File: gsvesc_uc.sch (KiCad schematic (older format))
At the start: 13 parts, among them U1 STM32F405RGTx, Y1 X50328MSB2GI

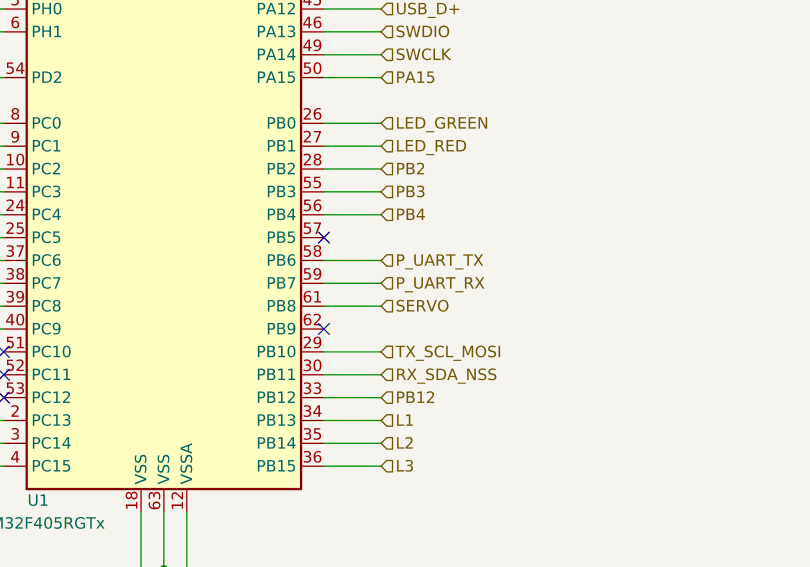
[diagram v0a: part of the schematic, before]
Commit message: Planes und Vias
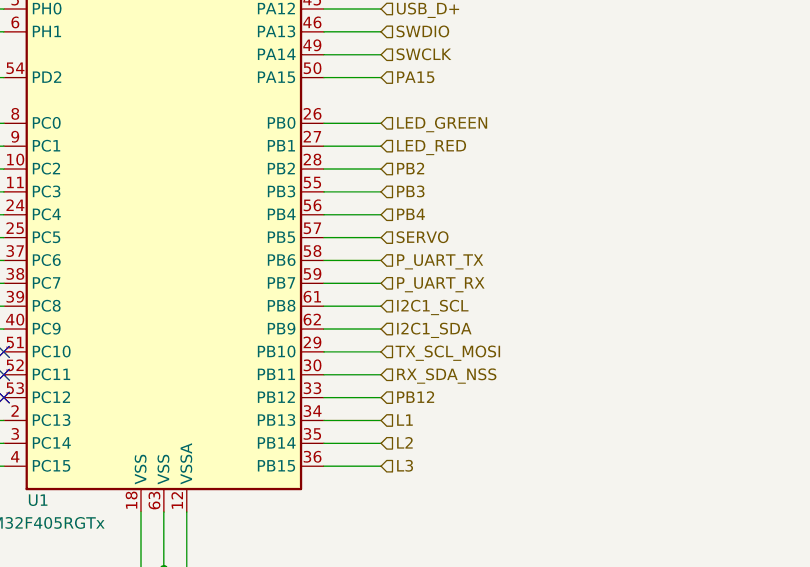
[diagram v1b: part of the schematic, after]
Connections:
- net SERVO: now also U1.57 (PB5); no longer U1.61 (PB8)
- net I2C1_SDA: now reaches U1.62 (PB9)
- new net I2C1_SCL: U1.61 (PB8)
- no-connect marks 5 -> 3
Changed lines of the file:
@@
 Comment4 ""
 $EndDescr
-$Comp
-L MCU_ST_STM32F4:STM32F405RGTx U1
-U 1 1 5BFF9EEA
-P 4150 4200
-F 0 "U1" H 3600 2450 50  0000 C CNN
-F 1 "STM32F405RGTx" H 3600 2350 50  0000 C CNN
-F 2 "Package_QFP:LQFP-64_10x10mm_P0.5mm" H 3550 2500 50  0001 R CNN
-F 3 "http://www.st.com/st-web-ui/static/active/en/resource/technical/document/datasheet/DM00037051.pdf" H 4150 4200 50  0001 C CNN
-	1    4150 4200
-	1    0    0    -1
-$EndComp
 Text HLabel 5100 2600 2    50   Input ~ 0
 VOLTAGE_1
@@
 Text HLabel 5100 4400 2    50   Input ~ 0
 LED_RED
-Text HLabel 5100 5100 2    50   Input ~ 0
+Text HLabel 5100 4800 2    50   Input ~ 0
 SERVO
 Text HLabel 5100 5300 2    50   Input ~ 0
@@
 	4850 5000 5100 5000
 Wire Wire Line
-	5100 5100 4850 5100
+	5100 4800 4850 4800
 Wire Wire Line
 	5100 5300 4850 5300
@@
 Text HLabel 3150 5200 0    50   Input ~ 0
 SENS_FILTER_ON
-NoConn ~ 4850 4800
-NoConn ~ 4850 5200
 NoConn ~ 3450 5300
 NoConn ~ 3450 5400
@@
 	1700 3700 1900 3700
 Connection ~ 1900 3700
+$Comp
+L MCU_ST_STM32F4:STM32F405RGTx U1
+U 1 1 5BFF9EEA
+P 4150 4200
+F 0 "U1" H 3600 2450 50  0000 C CNN
+F 1 "STM32F405RGTx" H 3600 2350 50  0000 C CNN
+F 2 "Package_QFP:LQFP-64_10x10mm_P0.5mm" H 3550 2500 50  0001 R CNN
+F 3 "http://www.st.com/st-web-ui/static/active/en/resource/technical/document/datasheet/DM00037051.pdf" H 4150 4200 50  0001 C CNN
+	1    4150 4200
+	1    0    0    -1
+$EndComp
+Wire Wire Line
+	4850 5100 5100 5100
+Wire Wire Line
+	4850 5200 5100 5200
+Text HLabel 5100 5100 2    50   Input ~ 0
+I2C1_SCL
+Text HLabel 5100 5200 2    50   Input ~ 0
+I2C1_SDA
 $EndSCHEMATC

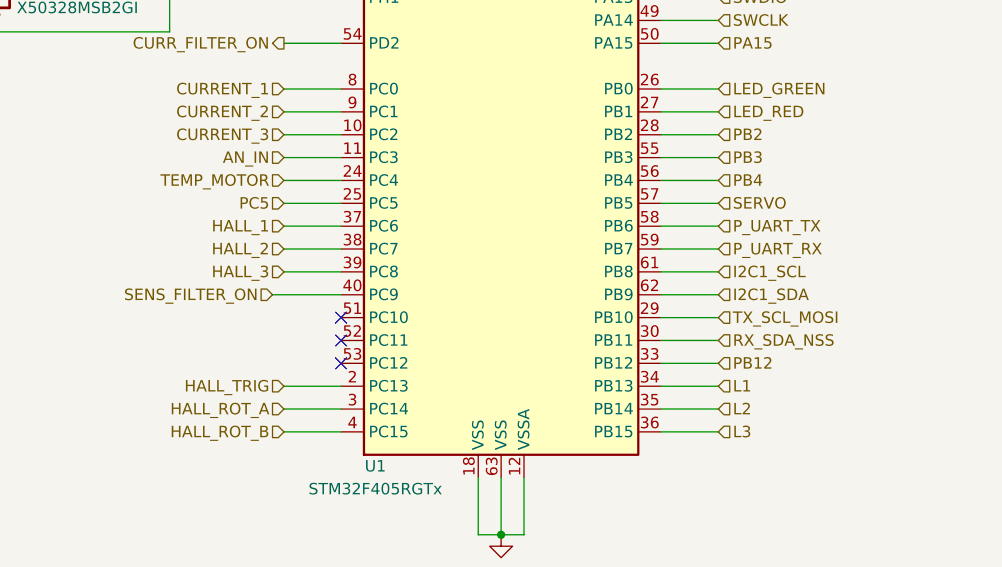
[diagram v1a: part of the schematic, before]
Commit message: BUG Fixes, see BUGS.txt
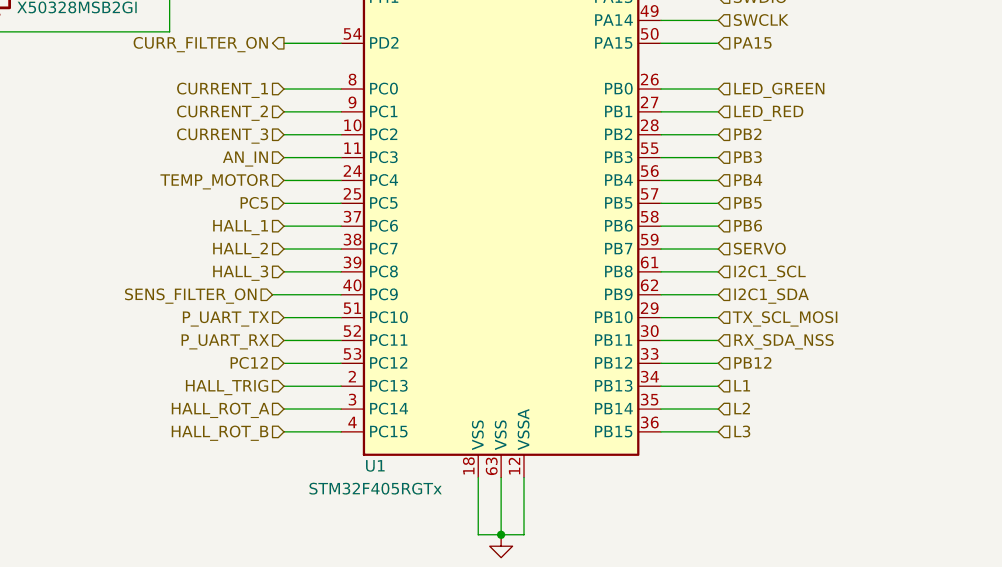
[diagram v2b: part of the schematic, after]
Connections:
- net P_UART_RX: now also U1.52 (PC11); no longer U1.59 (PB7)
- net P_UART_TX: now also U1.51 (PC10); no longer U1.58 (PB6)
- net SERVO: now also U1.59 (PB7); no longer U1.57 (PB5)
- net PC12: now reaches U1.53 (PC12)
- new net PB5: U1.57 (PB5)
- new net PB6: U1.58 (PB6)
- no-connect marks 3 -> 0
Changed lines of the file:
@@
 Text HLabel 5100 4400 2    50   Input ~ 0
 LED_RED
-Text HLabel 5100 4800 2    50   Input ~ 0
+Text HLabel 5100 5000 2    50   Input ~ 0
 SERVO
 Text HLabel 5100 5300 2    50   Input ~ 0
@@
 	5100 4400 4850 4400
 Wire Wire Line
-	4850 4600 5100 4600
-Wire Wire Line
-	5100 4700 4850 4700
-Wire Wire Line
-	4850 4900 5100 4900
-Wire Wire Line
-	4850 5000 5100 5000
-Wire Wire Line
-	5100 4800 4850 4800
+	4850 4800 5100 4800
+Wire Wire Line
+	5100 4900 4850 4900
+Wire Wire Line
+	3450 5300 3200 5300
+Wire Wire Line
+	3450 5400 3200 5400
+Wire Wire Line
+	5100 5000 4850 5000
 Wire Wire Line
 	5100 5300 4850 5300
@@
 	1    0    0    -1
 $EndComp
-Text HLabel 5100 4600 2    50   Input ~ 0
-PB3
-Text HLabel 5100 4700 2    50   Input ~ 0
-PB4
+Text HLabel 5100 4800 2    50   Input ~ 0
+PB5
 Text HLabel 5100 4900 2    50   Input ~ 0
+PB6
+Text HLabel 3200 5300 0    50   Input ~ 0
 P_UART_TX
-Text HLabel 5100 5000 2    50   Input ~ 0
+Text HLabel 3200 5400 0    50   Input ~ 0
 P_UART_RX
 Text HLabel 5100 5500 2    50   Input ~ 0
@@
 Text HLabel 3150 5200 0    50   Input ~ 0
 SENS_FILTER_ON
-NoConn ~ 3450 5300
-NoConn ~ 3450 5400
-NoConn ~ 3450 5500
 $Comp
 L Device:Crystal Y1
@@
 Text HLabel 5100 5200 2    50   Input ~ 0
 I2C1_SDA
+Wire Wire Line
+	4850 4600 5100 4600
+Wire Wire Line
+	5100 4700 4850 4700
+Text HLabel 5100 4600 2    50   Input ~ 0
+PB3
+Text HLabel 5100 4700 2    50   Input ~ 0
+PB4
+Wire Wire Line
+	3200 5500 3450 5500
+Text HLabel 3200 5500 0    50   Input ~ 0
+PC12
 $EndSCHEMATC
